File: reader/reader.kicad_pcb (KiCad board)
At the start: 2 copper layers, 77.5 x 80 mm, 64 parts, among them J1 USB_B_Mini, J2 swd, J3 Conn_01x06, J4 v_sup, Q1 CPH3350-TL-W, SW1 SW_Push, U1 BA33BC0FP-E2, U2 ST25R95, U3 STM32G051GxU, U4 FC2004C03-NSWBBW-91*E, Y1 27.12MHz

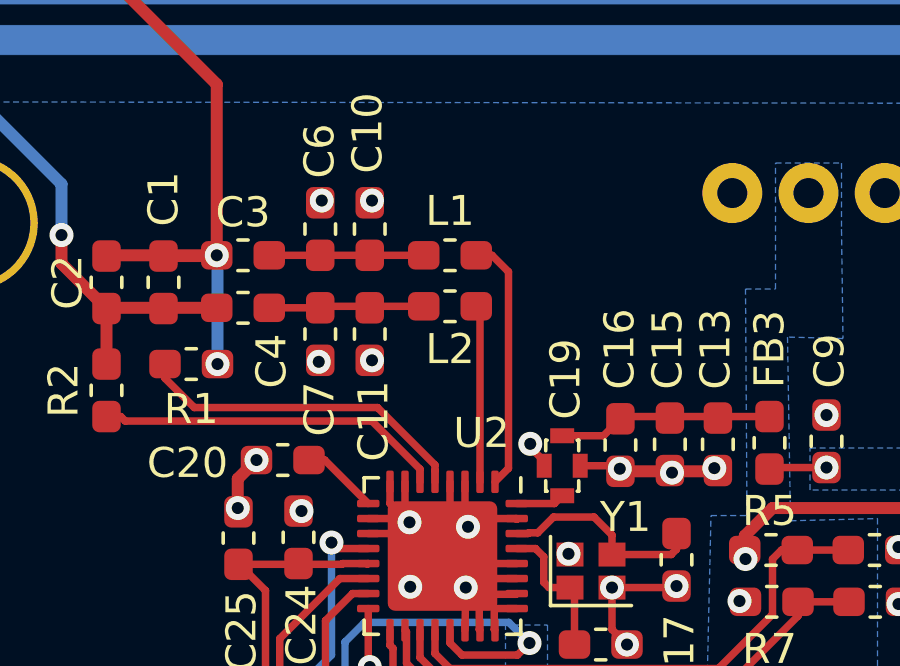
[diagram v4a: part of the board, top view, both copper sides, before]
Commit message: fix footprint of inductor
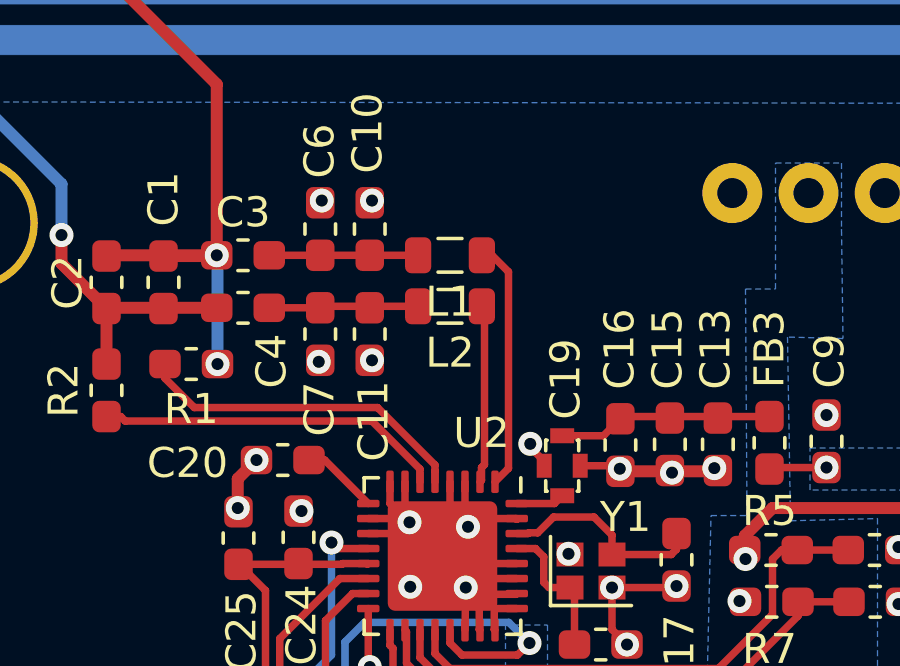
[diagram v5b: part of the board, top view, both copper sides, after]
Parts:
- L1, L2: footprint Inductor_SMD:L_0603_1608Metric_Pad1.05x0.95mm_HandSolder -> Inductor_SMD:L_0805_2012Metric

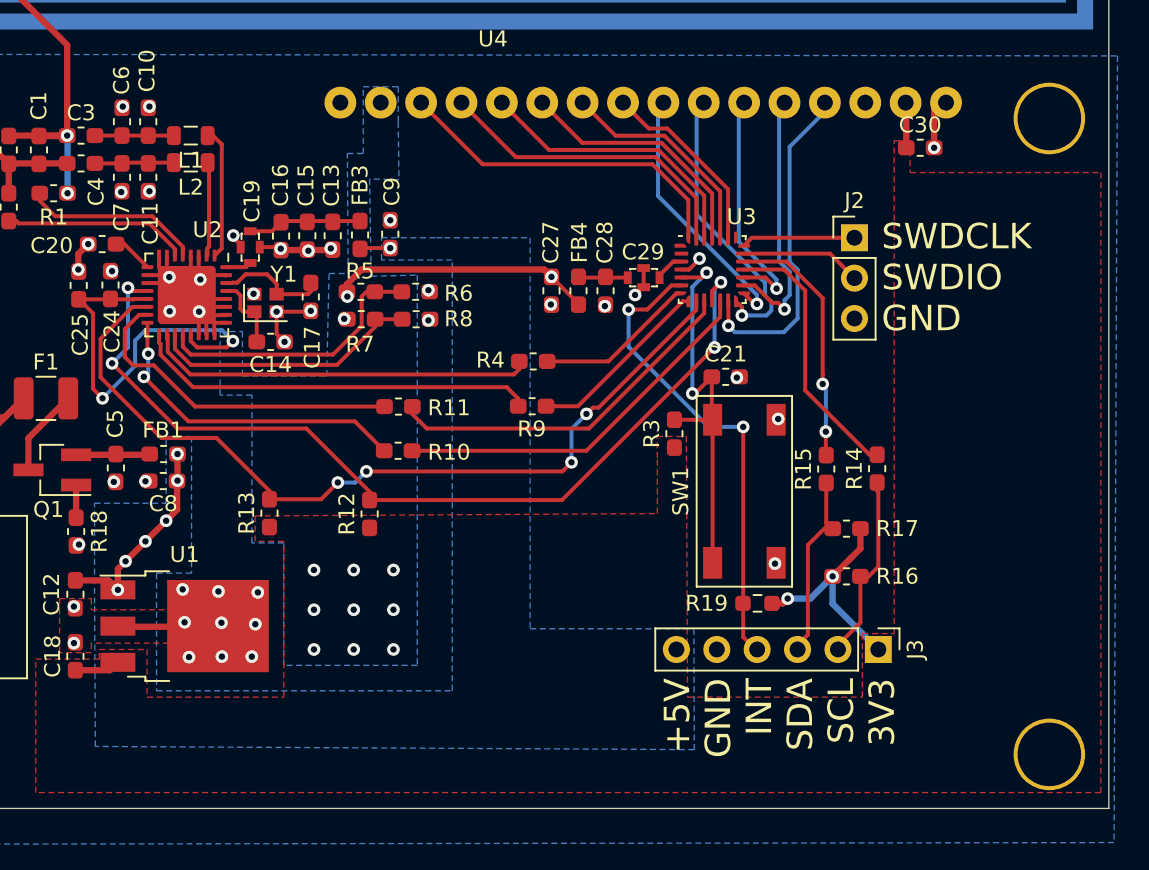
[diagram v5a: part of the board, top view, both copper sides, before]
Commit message: Add proper mcu pinout and uart as output
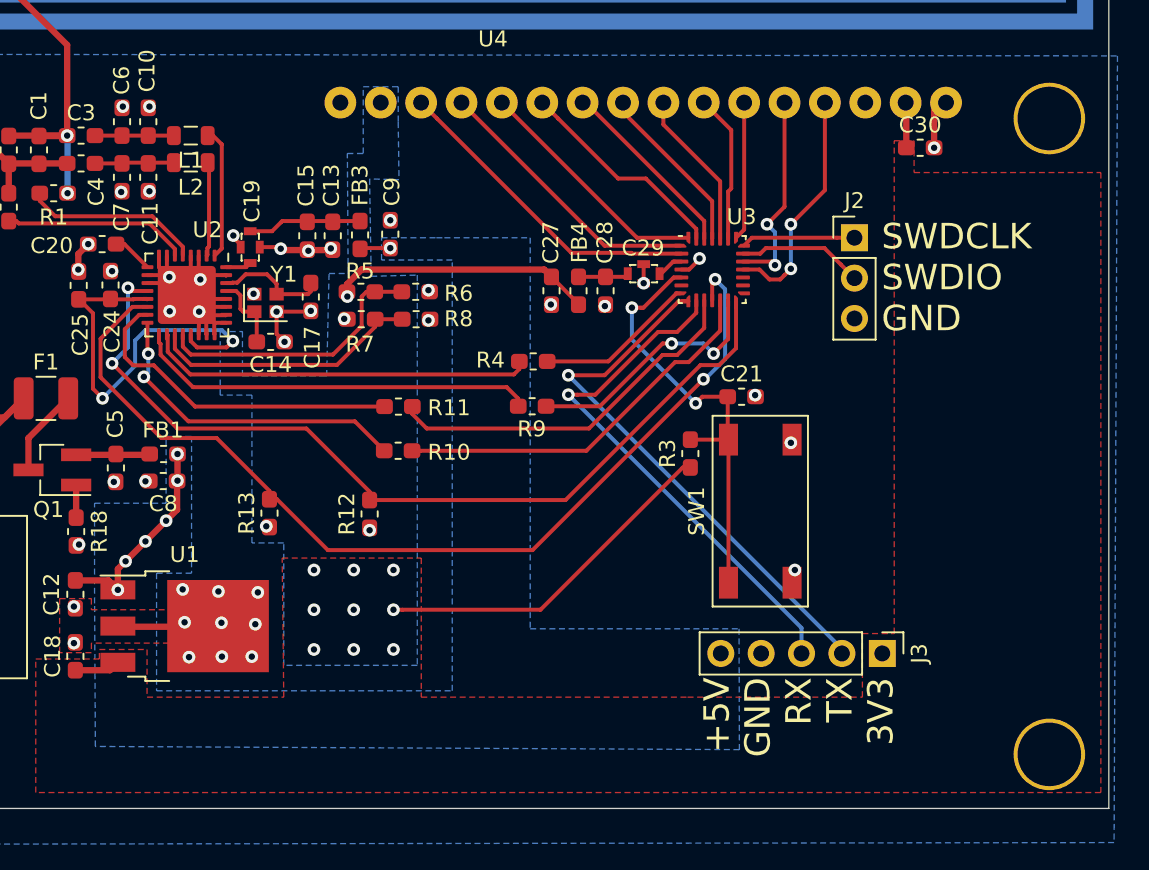
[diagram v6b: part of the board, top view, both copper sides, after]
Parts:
- removed C16: 10n, Capacitor_SMD:C_0603_1608Metric_Pad1.05x0.95mm_HandSolder
- removed R14, R15: 0, Resistor_SMD:R_0603_1608Metric_Pad1.05x0.95mm_HandSolder
- removed R16, R17: 2k2, Resistor_SMD:R_0603_1608Metric_Pad1.05x0.95mm_HandSolder
- removed R19: 2k2, Resistor_SMD:R_0603_1608Metric_Pad0.98x0.95mm_HandSolder
- J3: value Conn_01x06 -> Conn_01x05; footprint Connector_PinHeader_2.54mm:PinHeader_1x06_P2.54mm_Vertical -> Connector_PinHeader_2.54mm:PinHeader_1x05_P2.54mm_Vertical
- moved C21 1.60 mm to (164.4, 114.1)
- moved R3 1.60 mm to (161.2, 117.7)
- moved SW1 1.60 mm to (165.6, 121.3)
- moved J3 0.35 mm to (173.2, 130.2)
- moved C29 0.25 mm to (158.2, 106.4)
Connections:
- J1 pad 2: Net-(J1-Pad2) -> (no net)
- J1 pad 3: Net-(J1-Pad3) -> (no net)
- J1 pad 4: Net-(J1-Pad4) -> (no net)
- J3 pad 2: /i2c_scl_t -> to_keypad_tx
- J3 pad 3: /i2c_sda_t -> from_keypad_rx
- J3 pad 4: keypad_int -> GND
- J3 pad 5: GND -> +5V
- U3 pad 1: Net-(U3-Pad1) -> lcd_d6
- U3 pad 11: nfc_irq_in -> nfc_irq_out
- U3 pad 13: lcd_rs -> spi_mosi
- U3 pad 14: /lcd_d0 -> nfc_irq_in
- U3 pad 15: /lcd_d1 -> (no net)
- U3 pad 16: lcd_rw -> (no net)
- U3 pad 17: lcd_e -> (no net)
- U3 pad 18: i2c_scl -> lcd_rs
- U3 pad 19: i2c_sda -> lcd_rw
- U3 pad 2: Net-(U3-Pad2) -> lcd_d7
- U3 pad 22: Net-(U3-Pad22) -> lcd_e
- U3 pad 23: /lcd_d2 -> lcd_d0
- U3 pad 24: /lcd_d3 -> lcd_d1
- U3 pad 25: /lcd_d4 -> lcd_d2
- U3 pad 26: /lcd_d5 -> lcd_d3
- U3 pad 27: /lcd_d6 -> lcd_d4
- U3 pad 28: /lcd_d7 -> lcd_d5
- U3 pad 6: keypad_int -> (no net)
- U3 pad 8: spi_mosi -> to_keypad_tx
- U3 pad 9: nfc_irq_out -> from_keypad_rx
- U4 pad 10: /lcd_d3 -> lcd_d3
- U4 pad 11: /lcd_d4 -> lcd_d4
- U4 pad 12: /lcd_d5 -> lcd_d5
- U4 pad 13: /lcd_d6 -> lcd_d6
- U4 pad 14: /lcd_d7 -> lcd_d7
- U4 pad 3: Net-(U4-Pad3) -> (no net)
- U4 pad 7: /lcd_d0 -> lcd_d0
- U4 pad 8: /lcd_d1 -> lcd_d1
- U4 pad 9: /lcd_d2 -> lcd_d2
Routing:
- net to_keypad_tx: track 0.00 -> 34.5 mm, vias 0 -> 1
- net from_keypad_rx: track 0.00 -> 33.3 mm, vias 0 -> 1
- net keypad_int: track 29.8 -> 0.00 mm, vias 2 -> 0
- net /lcd_d7: track 22.2 -> 0.00 mm
- net lcd_d7: track 0.00 -> 20.3 mm
- net /lcd_d6: track 20.3 -> 0.00 mm
- net /lcd_d0: track 18.5 -> 0.00 mm, vias 1 -> 0
- net /lcd_d5: track 18.3 -> 0.00 mm
- net lcd_d6: track 0.00 -> 17.5 mm
- net i2c_scl: track 16.9 -> 0.00 mm
- net /lcd_d1: track 16.7 -> 0.00 mm, vias 1 -> 0
- net /lcd_d4: track 16.4 -> 0.00 mm
- net i2c_sda: track 15.9 -> 0.00 mm, vias 2 -> 0
- net lcd_d5: track 0.00 -> 15.3 mm
- net /lcd_d3: track 14.4 -> 0.00 mm
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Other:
- board text added: "+5V GND RX TX 3V3"
- board text removed: "+5V GND INT SDA SCL 3V3"
